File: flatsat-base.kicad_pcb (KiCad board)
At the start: 2 copper layers, 254 x 152.4 mm, 13 parts, among them J1 xf2m-2415-1a-symbols, J10 Conn_01x24_Male, J11 Conn_02x05_Odd_Even, J12 Conn_02x05_Odd_Even, J13 Conn_01x10_Male, J2 XF2M-1015-1A-symbols, J3 XF2M-1015-1A-symbols, J4 XF2M-1015-1A-symbols, J5 XF2M-1015-1A-symbols, J6 XF2M-1015-1A-symbols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

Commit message: Shrank board size a little for cheaper production
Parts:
- removed J2, J9: XF2M-1015-1A-symbols, PyCubed-Mini Solar:XF2M-1015-1A
- added REF**: X Label, X Label, F.Cu at (52.2, 45.5)
- added REF**: X Label, X Label, F.Cu at (51.8, 100.1)
- added Ref**: Val**, custom-footprints:ypanel, F.Cu at (105.7, 44.7)
- added Ref**: Val**, custom-footprints:ypanel, F.Cu at (106.0, 98.2)
- added Ref**: Val**, custom-footprints:ypanel, F.Cu at (177.6, 44.7)
- added Ref**: Val**, custom-footprints:ypanel, F.Cu at (184.2, 103.8)
- J11: moved to B.Cu
- moved J4 142.3 mm to (45.3, 135.3), turned to 180 degrees
- moved J13 121.0 mm to (293.6, 131.3)
- moved J10 121.0 mm to (309.1, 131.3)
- moved J6 111.3 mm to (207.5, 113.2), turned to -90 degrees
- moved J1 80.8 mm to (200.2, 37.1), turned to 90 degrees
- moved J8 80.5 mm to (112.6, 135.3)
- moved J12 66.1 mm to (215.6, 91.9)
- moved J5 61.0 mm to (160.2, 7.99)
- moved J11 57.4 mm to (216.3, 45.5), turned to 180 degrees
- moved J7 52.2 mm to (105.6, 7.99)
- moved J3 26.4 mm to (58.9, 7.99)
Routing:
- net +3V3: track 59.7 -> 0.00 mm
- net GND: track 58.0 -> 0.00 mm
- net COIL4_P: track 56.4 -> 0.00 mm
- net COIL4_N: track 54.8 -> 0.00 mm
- net COIL3_N: track 53.2 -> 0.00 mm
- net COIL3_P: track 51.6 -> 0.00 mm
- net COIL2_P: track 50.1 -> 0.00 mm
- net COIL2_N: track 48.5 -> 0.00 mm
- net COIL1_N: track 46.9 -> 0.00 mm
- net COIL1_P: track 44.5 -> 0.00 mm
- net BATT_N: track 42.9 -> 0.00 mm
- net BATT_P: track 40.9 -> 0.00 mm
- added copper zone on F.Cu, net GND
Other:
- board size 254 x 152.4 mm -> 228.6 x 134.6 mm
- board text added: "cameraboard"
- board text added: "mainboard"
- board text removed: "+X"
- board text removed: "+Y"
- board text removed: "+Z"
- board text removed: "-X"
- board text removed: "-Y"
- board text removed: "-Z"
- board text removed: "Camera"
- board text removed: "Mainboard"

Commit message: Partially routed
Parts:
- J1: value xf2m-2415-1a-symbols -> FFC2B28-24-G; footprint PyCubed-Mini Main:XF2M-2415-1A -> mainboard:GCT_FFC2B28-24-G
- J2: renamed from J3; value XF2M-1015-1A-symbols -> FFC2B28-10-G; footprint PyCubed-Mini Solar:XF2M-1015-1A -> solarpanels:GCT_FFC2B28-10-G
- J3: renamed from J4; value XF2M-1015-1A-symbols -> FFC2B28-10-G; footprint PyCubed-Mini Solar:XF2M-1015-1A -> solarpanels:GCT_FFC2B28-10-G
- J4: renamed from J5; value XF2M-1015-1A-symbols -> FFC2B28-10-G; footprint PyCubed-Mini Solar:XF2M-1015-1A -> solarpanels:GCT_FFC2B28-10-G
- J5: renamed from J6; value XF2M-1015-1A-symbols -> FFC2B28-10-G; footprint PyCubed-Mini Solar:XF2M-1015-1A -> solarpanels:GCT_FFC2B28-10-G
- J6: renamed from J7; value XF2M-1015-1A-symbols -> FFC2B28-10-G; footprint PyCubed-Mini Solar:XF2M-1015-1A -> solarpanels:GCT_FFC2B28-10-G
- J7: renamed from J8; value XF2M-1015-1A-symbols -> FFC2B28-10-G; footprint PyCubed-Mini Solar:XF2M-1015-1A -> solarpanels:GCT_FFC2B28-10-G
- J8: renamed from J11; footprint Connector_PinHeader_1.27mm:PinHeader_2x05_P1.27mm_Vertical -> Connector_PinSocket_1.27mm:PinSocket_2x05_P1.27mm_Vertical; moved to F.Cu
- moved J10 132.4 mm to (192.0, 69.6), turned to 180 degrees
- moved J11 49.2 mm to (244.6, 135.1)
- moved J9 4.94 mm to (216.4, 96.8), turned to 180 degrees
- moved J1 3.01 mm to (203.2, 37.1)
- moved J7 2.93 mm to (112.6, 132.3)
- moved J3 2.93 mm to (45.3, 132.3)
- moved J5 2.79 mm to (204.7, 113.2)
- moved J4 2.68 mm to (160.2, 10.7)
- moved J6 2.68 mm to (105.6, 10.7)
- moved J2 2.68 mm to (58.9, 10.7)
- turned J8 to 0 degrees
- renumbered J13 to J11, J12 to J9
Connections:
- J11 pad 10: CAM_P10 -> CAM_P3
- J11 pad 3: CAM_P3 -> GND
- J11 pad 4: GND -> SCK
- J11 pad 5: MOSI -> EN_CAM
- J11 pad 6: SCK -> CAM_P10
- J11 pad 7: MISO -> CS_CAM
- J11 pad 8: EN_CAM -> MISO
- J11 pad 9: CS_CAM -> MOSI
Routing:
- net BATT_P: track 0.00 -> 391.1 mm, vias 0 -> 3
- net BATT_N: track 0.00 -> 120.2 mm
- net SCL2: track 0.00 -> 117.4 mm
- net SDA2: track 0.00 -> 115.5 mm
- net SCK: track 0.00 -> 109.8 mm
- net EN_CAM: track 0.00 -> 103.0 mm
- net CAM_P10: track 0.00 -> 95.9 mm
- net CAM_P3: track 0.00 -> 93.2 mm
- net MOSI: track 0.00 -> 92.6 mm
- net MISO: track 0.00 -> 92.2 mm
- net CS_CAM: track 0.00 -> 91.8 mm
- net COIL6_P: track 0.00 -> 28.0 mm
- net COIL6_N: track 0.00 -> 26.1 mm
- net +3V3: track 0.00 -> 24.6 mm, vias 0 -> 1
- net COIL5_P: track 0.00 -> 24.2 mm
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- added copper zone on B.Cu, net +3V3

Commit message: Finished routing
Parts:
- added H1: MountingHole, MountingHole:MountingHole_3.2mm_M3_DIN965_Pad, F.Cu at (27.9, 9.65)
- added H2: MountingHole, MountingHole:MountingHole_3.2mm_M3_DIN965_Pad, F.Cu at (27.9, 134.1)
- added H3: MountingHole, MountingHole:MountingHole_3.2mm_M3_DIN965_Pad, F.Cu at (246.4, 134.1)
- added H4: MountingHole, MountingHole:MountingHole_3.2mm_M3_DIN965_Pad, F.Cu at (246.4, 9.65)
- added Ref**: Val**, custom-footprints:pycubed_mini_logo, F.Cu at (235.1, 13.2)
- moved J10 58.5 mm to (188.7, 11.2), turned to 0 degrees
- moved J11 7.63 mm to (237.0, 135.1)
- moved J1 1.02 mm to (202.2, 37.1)
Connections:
- J1 pad 1: SCL2 -> BATT_P
- J1 pad 10: SCL1 -> COIL4_P
- J1 pad 11: BATT_STAT -> GND
- J1 pad 14: GND -> BATT_STAT
- J1 pad 15: COIL4_P -> SCL1
- J1 pad 16: COIL4_N -> SDA1
- J1 pad 17: COIL3_N -> BURN2
- J1 pad 18: COIL3_P -> BURN1
- J1 pad 19: COIL2_P -> COIL5_N
- J1 pad 2: SDA2 -> BATT_N
- J1 pad 20: COIL2_N -> COIL5_P
- J1 pad 21: COIL1_N -> COIL6_N
- J1 pad 22: COIL1_P -> COIL6_P
- J1 pad 23: BATT_N -> SDA2
- J1 pad 24: BATT_P -> SCL2
- J1 pad 3: COIL6_P -> COIL1_P
- J1 pad 4: COIL6_N -> COIL1_N
- J1 pad 5: COIL5_P -> COIL2_N
- J1 pad 6: COIL5_N -> COIL2_P
- J1 pad 7: BURN1 -> COIL3_P
- J1 pad 8: BURN2 -> COIL3_N
- J1 pad 9: SDA1 -> COIL4_N
- J2 pad 10: COIL3_P -> COIL5_P
- J2 pad 3: SDA2 -> SDA1
- J2 pad 4: SCL2 -> SCL1
- J2 pad 9: COIL3_N -> COIL5_N
- J3 pad 10: COIL4_P -> COIL6_P
- J3 pad 3: SDA1 -> SDA2
- J3 pad 4: SCL1 -> SCL2
- J3 pad 9: COIL4_N -> COIL6_N
- J4 pad 10: COIL5_P -> COIL1_P
- J4 pad 5: BURN1 -> unconnected-(J4-Pad5)
- J4 pad 9: COIL5_N -> COIL1_N
- J5 pad 10: COIL6_P -> COIL2_P
- J5 pad 9: COIL6_N -> COIL2_N
- J6 pad 10: COIL1_P -> COIL3_P
- J6 pad 9: COIL1_N -> COIL3_N
- J7 pad 10: COIL2_P -> COIL4_P
- J7 pad 5: unconnected-(J7-Pad5) -> BURN1
- J7 pad 9: COIL2_N -> COIL4_N
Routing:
- net BATT_N: track 120.2 -> 473.9 mm, vias 0 -> 3
- net COIL6_P: track 28.0 -> 317.5 mm, vias 0 -> 1
- net COIL6_N: track 26.1 -> 311.3 mm, vias 0 -> 1
- net SCL2: track 117.4 -> 342.2 mm
- net SDA2: track 115.5 -> 337.6 mm
- net BURN1: track 20.3 -> 229.6 mm, vias 0 -> 2
- net SCL1: track 14.5 -> 213.2 mm
- net SDA1: track 16.4 -> 213.3 mm
- net COIL4_P: track 10.7 -> 206.3 mm, vias 0 -> 1
- net COIL4_N: track 11.5 -> 203.9 mm, vias 0 -> 1
- net BATT_P: track 391.1 -> 552.2 mm
- net COIL5_N: track 22.2 -> 158.3 mm, vias 0 -> 1
- net COIL5_P: track 24.2 -> 157.3 mm, vias 0 -> 1
- net COIL3_P: track 14.9 -> 142.3 mm, vias 0 -> 1
- net COIL3_N: track 13.0 -> 139.7 mm, vias 0 -> 1
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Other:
- board text added: "+3V3"
- board text added: "BATT_N"
- board text added: "BATT_P"
- board text added: "BATT_STAT"
- board text added: "BURN1"
- board text added: "BURN2"
- board text added: "COIL1_N"
- board text added: "COIL1_P"
- board text added: "COIL2_N"
- board text added: "COIL2_P"
- board text added: "COIL3_N"
- board text added: "COIL3_P"
- board text added: "COIL4_N"
- board text added: "COIL4_P"
- board text added: "COIL5_N"
- board text added: "COIL5_P"
- board text added: "COIL6_N"
- board text added: "COIL6_P"
- board text added: "CS_CAM"
- board text added: "EN_CAM"
- board text added: "GND"
- board text added: "MISO"
- board text added: "MOSI"
- board text added: "SCK"
- board text added: "SCL1"
- board text added: "SCL2"
- board text added: "SDA1"
- board text added: "SDA2"

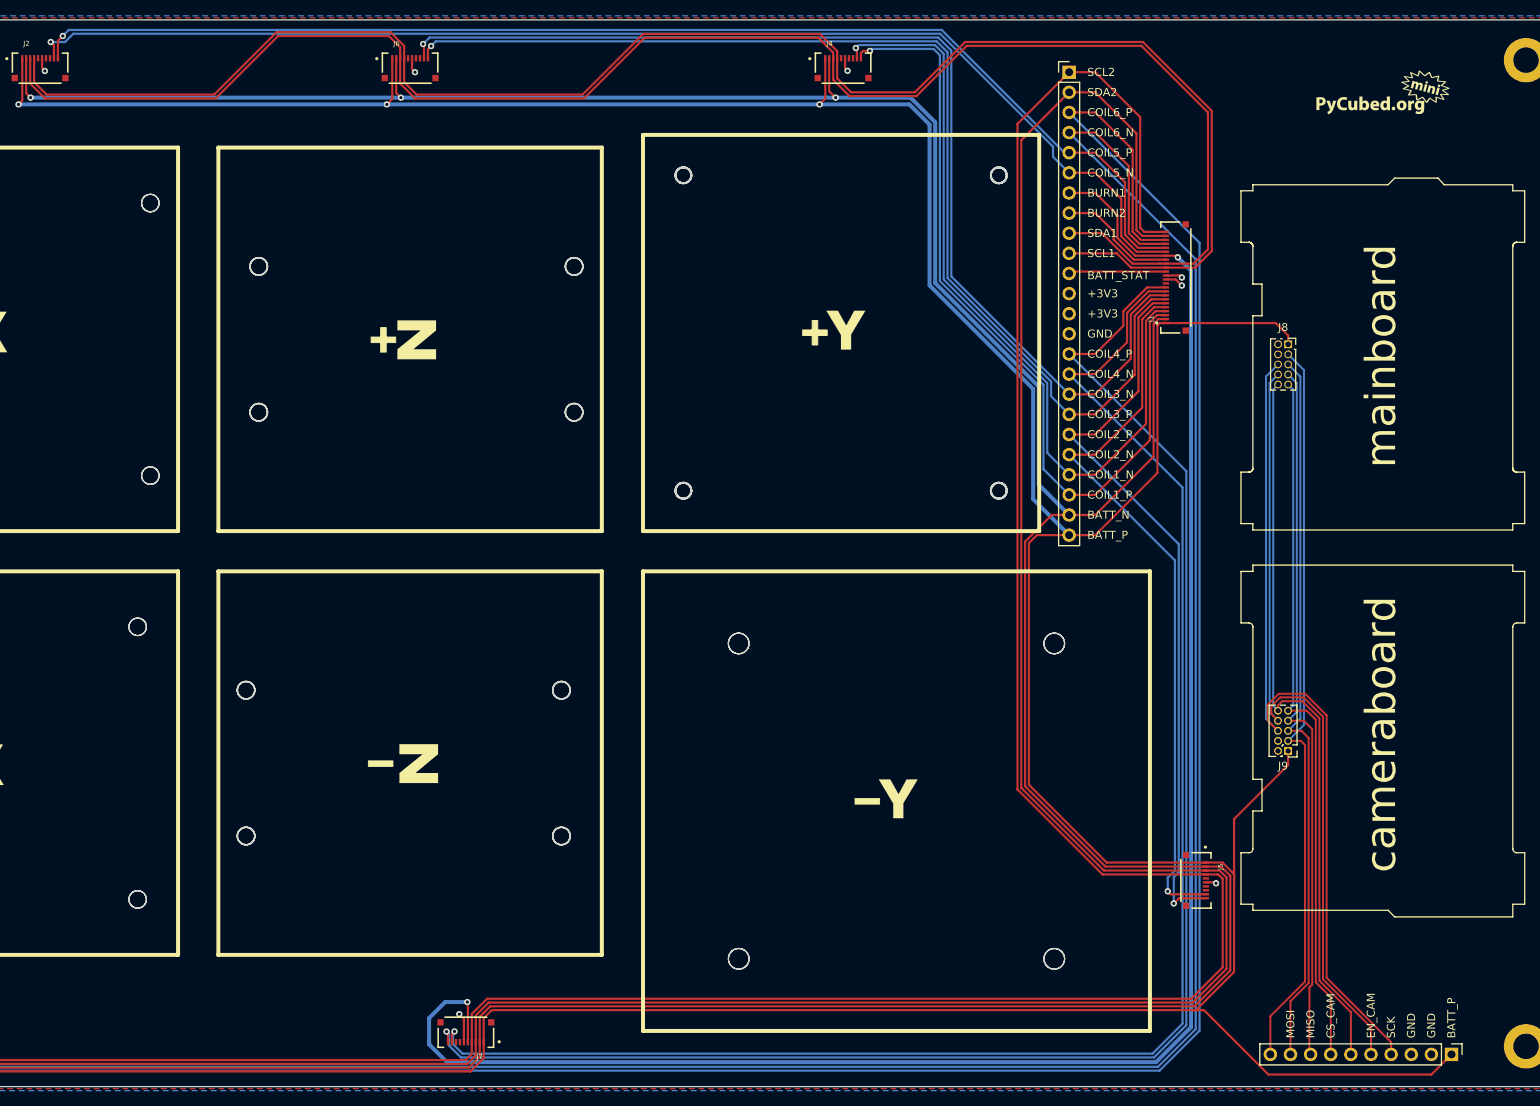
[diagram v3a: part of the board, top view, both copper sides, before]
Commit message: Fixed Pinout on mainboard connector, added redundant flat-flex connector
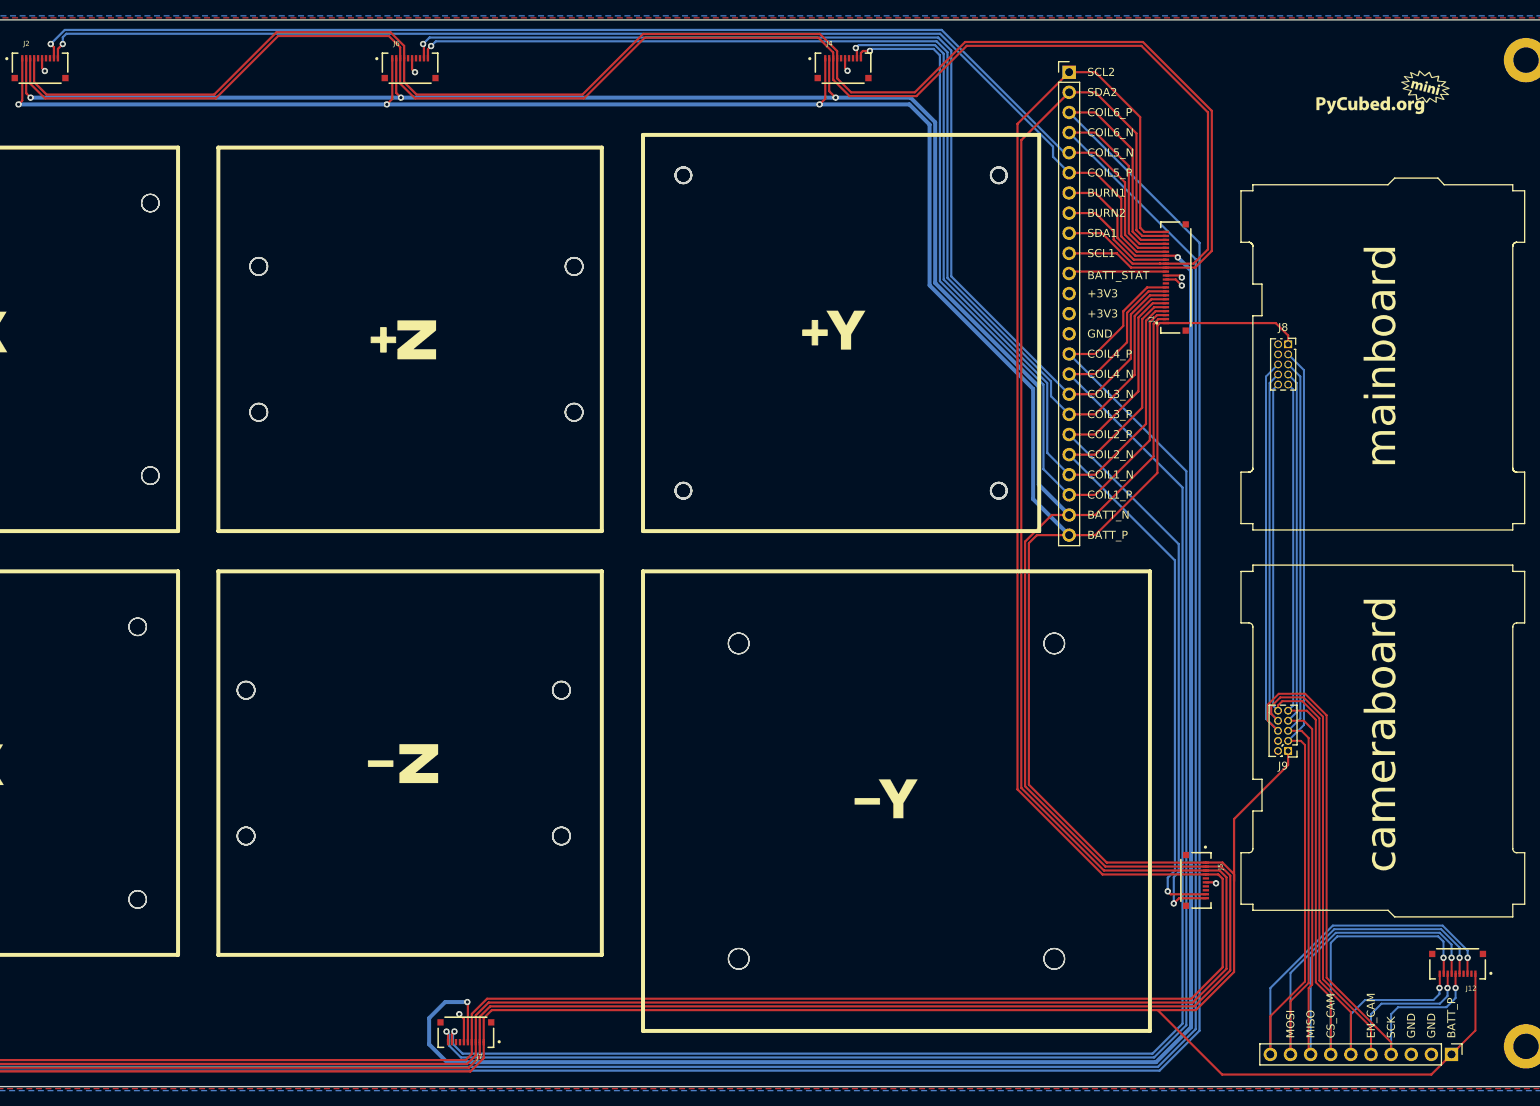
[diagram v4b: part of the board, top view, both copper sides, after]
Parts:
- added J12: FFC2B28-10-G, solarpanels:GCT_FFC2B28-10-G, F.Cu at (237.7, 123.7)
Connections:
- J1 pad 19: COIL5_N -> COIL5_P
- J1 pad 20: COIL5_P -> COIL5_N
- J10 pad 5: COIL5_P -> COIL5_N
- J10 pad 6: COIL5_N -> COIL5_P
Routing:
- net CAM_P3: track 93.6 -> 134.4 mm, vias 0 -> 1
- net MOSI: track 91.4 -> 129.5 mm, vias 0 -> 1
- net MISO: track 89.1 -> 124.8 mm, vias 0 -> 1
- net CS_CAM: track 88.7 -> 121.6 mm, vias 0 -> 1
- net CAM_P10: track 92.7 -> 112.6 mm, vias 0 -> 1
- net EN_CAM: track 99.9 -> 118.4 mm, vias 0 -> 1
- net SCK: track 106.6 -> 123.7 mm, vias 0 -> 1
- net BATT_P: track 552.2 -> 568.0 mm

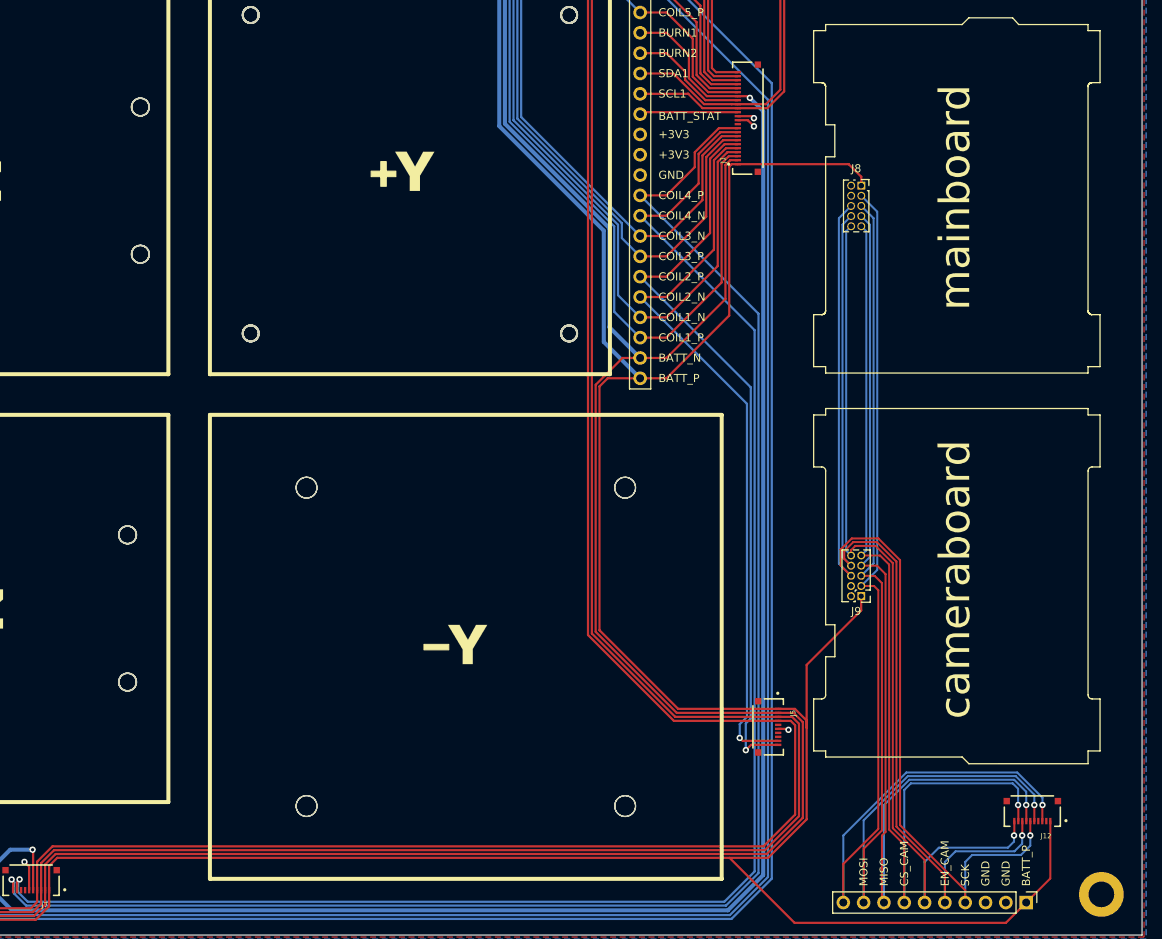
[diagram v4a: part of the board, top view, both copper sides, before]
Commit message: Added Mounting Holes on main and camera boards
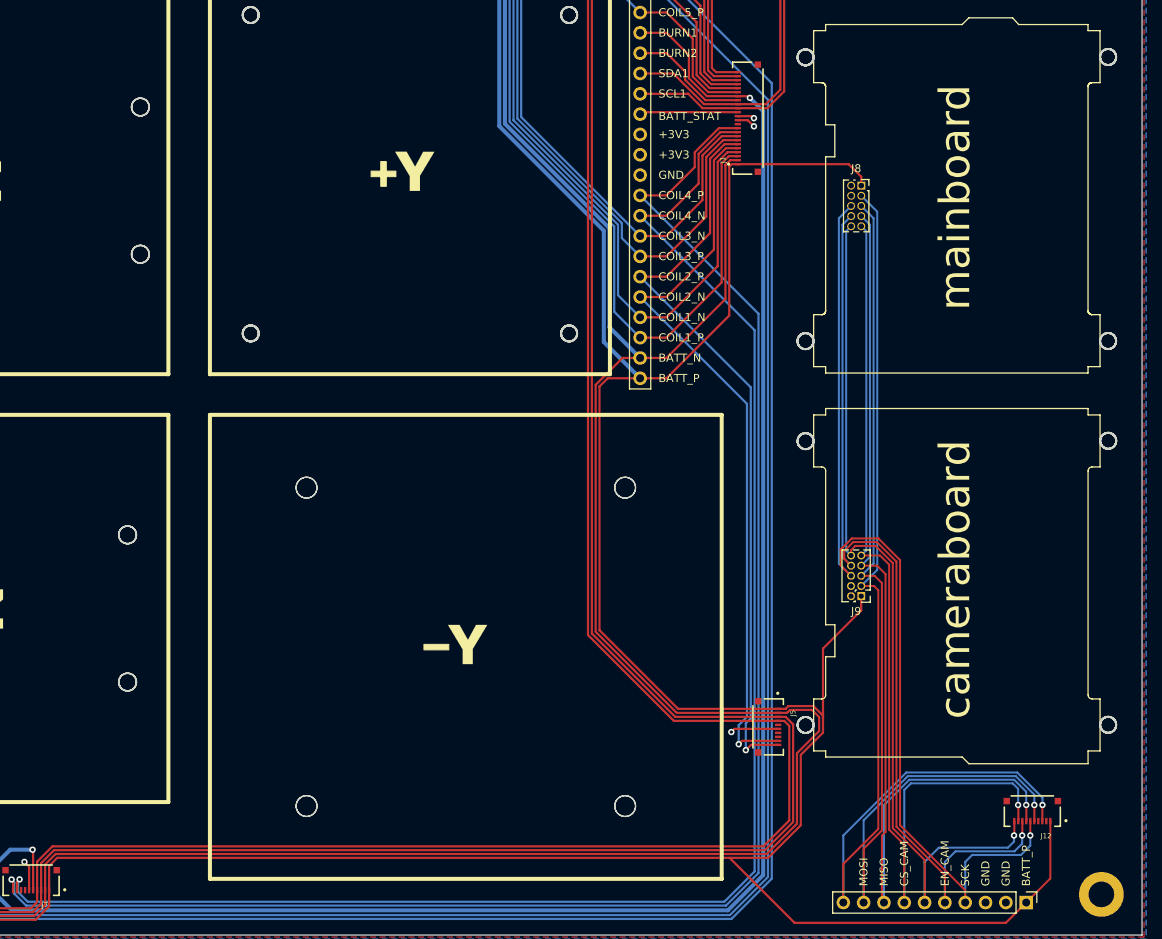
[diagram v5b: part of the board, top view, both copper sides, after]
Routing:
- net +3V3: track 17.5 -> 22.2 mm
- net BATT_N: track 473.9 -> 477.4 mm
- net BATT_P: track 568.0 -> 569.5 mm
- net SCL2: track 342.2 -> 341.1 mm
- net SDA2: track 337.6 -> 336.5 mm
- net COIL2_N: track 92.4 -> 93.4 mm
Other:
- outline, holes or cut-outs redrawn
